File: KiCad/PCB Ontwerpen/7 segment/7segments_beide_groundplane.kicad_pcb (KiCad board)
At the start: 2 copper layers, 72.4 x 55.9 mm, 25 parts, among them J1 Conn_01x04_Female, J2 12V DC, J3 R pinnen RGB strips, SW1 ENABLE, SW2 BOOT, T1 NTR4503, T2 NTR4503, T3 NTR4503, T4 NTR4503, T5 NTR4503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

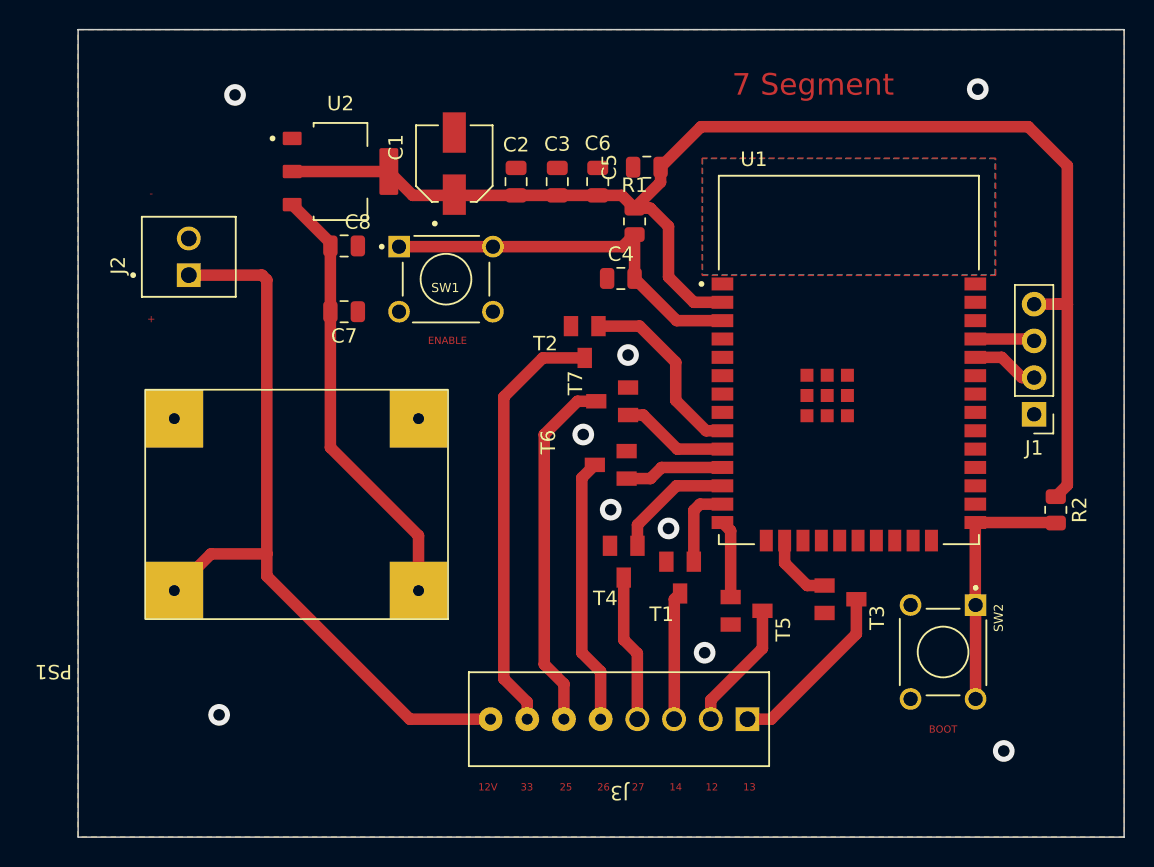
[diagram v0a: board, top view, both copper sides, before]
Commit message: aanpassing 7 segment naar dc jack
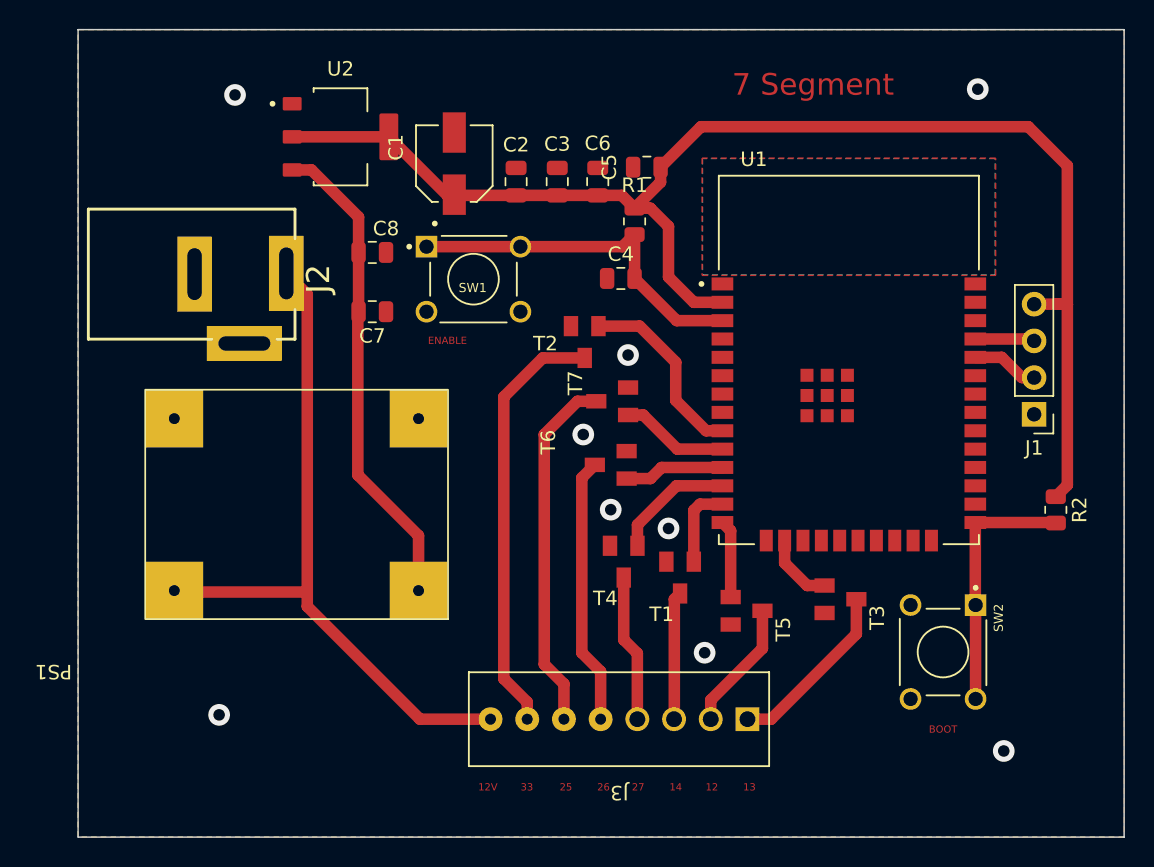
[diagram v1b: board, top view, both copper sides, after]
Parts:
- J2: value 12V DC -> DCJ200-10-A-XX-X_REVA; footprint libraries:TE_1546215-2 -> libraries:GCT_DCJ200-10-A-XX-X_REVA
- moved U2 2.40 mm to (122.3, 76.0)
- moved C8 2.00 mm to (124.5, 84.0)
- moved C7 1.95 mm to (124.5, 88.1)
- moved SW1 1.90 mm to (131.5, 85.8)
- moved J2 1.22 mm to (112.0, 85.5), turned to -90 degrees
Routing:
- net 12V: track 53.0 -> 48.8 mm
- net Net-(C7-Pad2): track 30.3 -> 33.6 mm
- net Net-(C4-Pad2): track 27.0 -> 25.1 mm
- net +3V3: track 95.9 -> 96.9 mm
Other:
- board text removed: "+"
- board text removed: "-"
